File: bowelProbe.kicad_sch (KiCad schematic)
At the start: 52 parts, among them J10 Conn_01x01, J11 Conn_01x01, J12 Conn_01x01, J13 Conn_01x01, J2 Conn_01x01, J3 Conn_01x01, J4 Conn_01x01, J5 Conn_01x01, J6 Conn_01x01, J7 Conn_01x01, J8 Conn_01x01, J9 Conn_01x01, U1 MAX038CPP, U2 OPA2134PA, U3 MCP6002-E/P, U4 TL072ACP

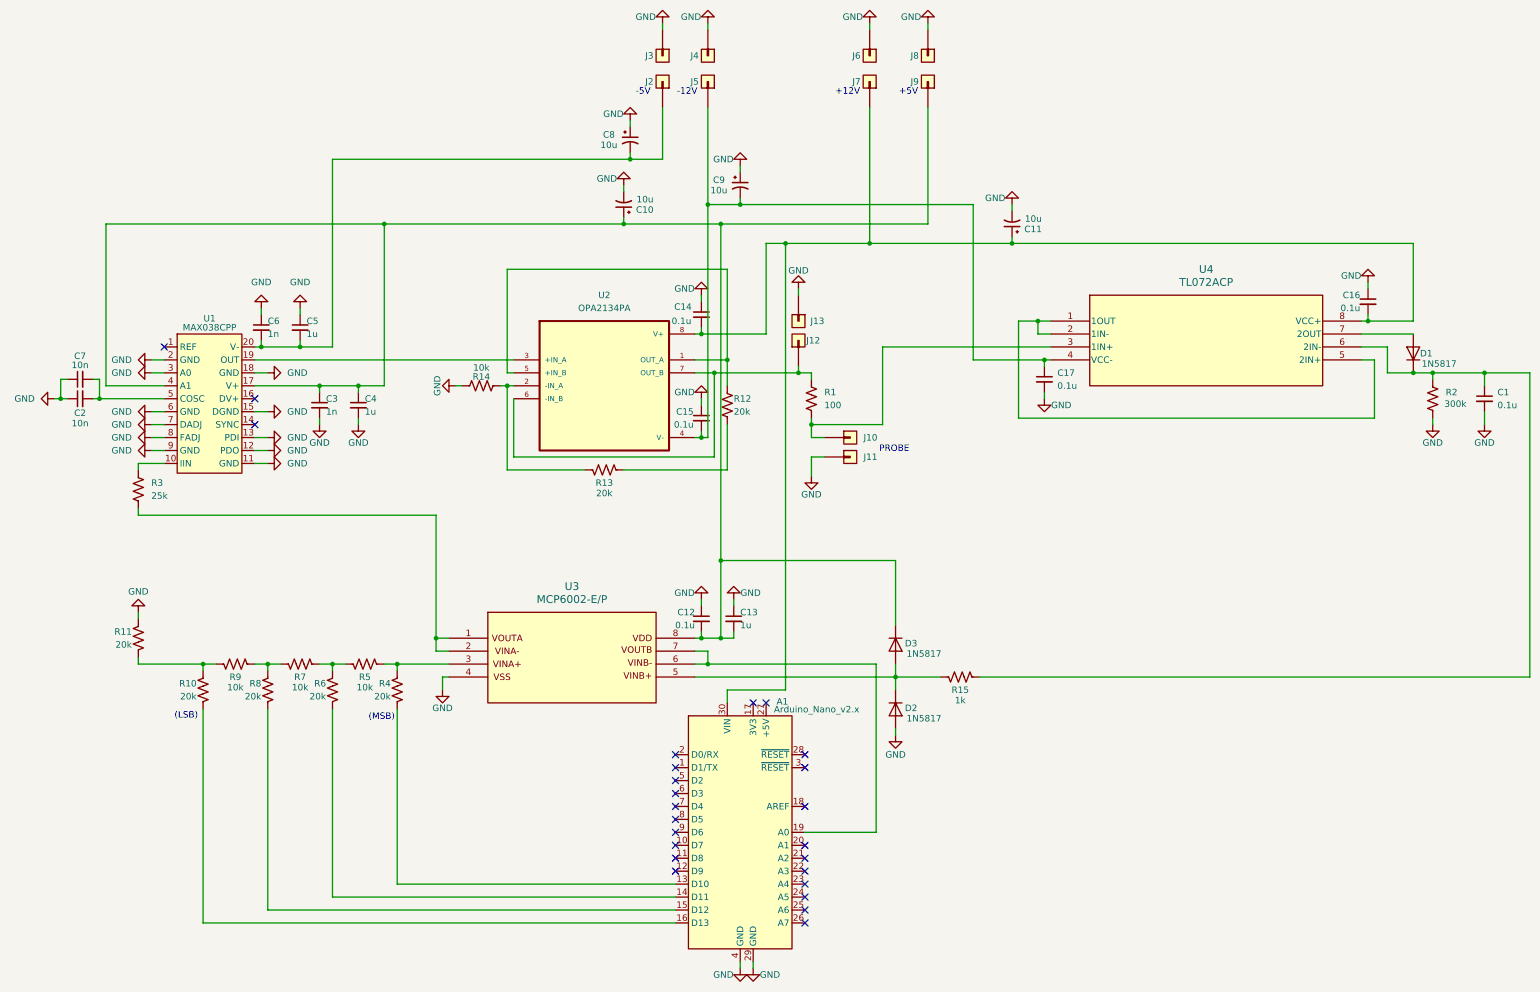
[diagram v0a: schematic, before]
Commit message: PCB Passed Final Check
Updated PCB reference designators (both in schematic and layout). Gave final check to ensure proper PCB layout and routing.
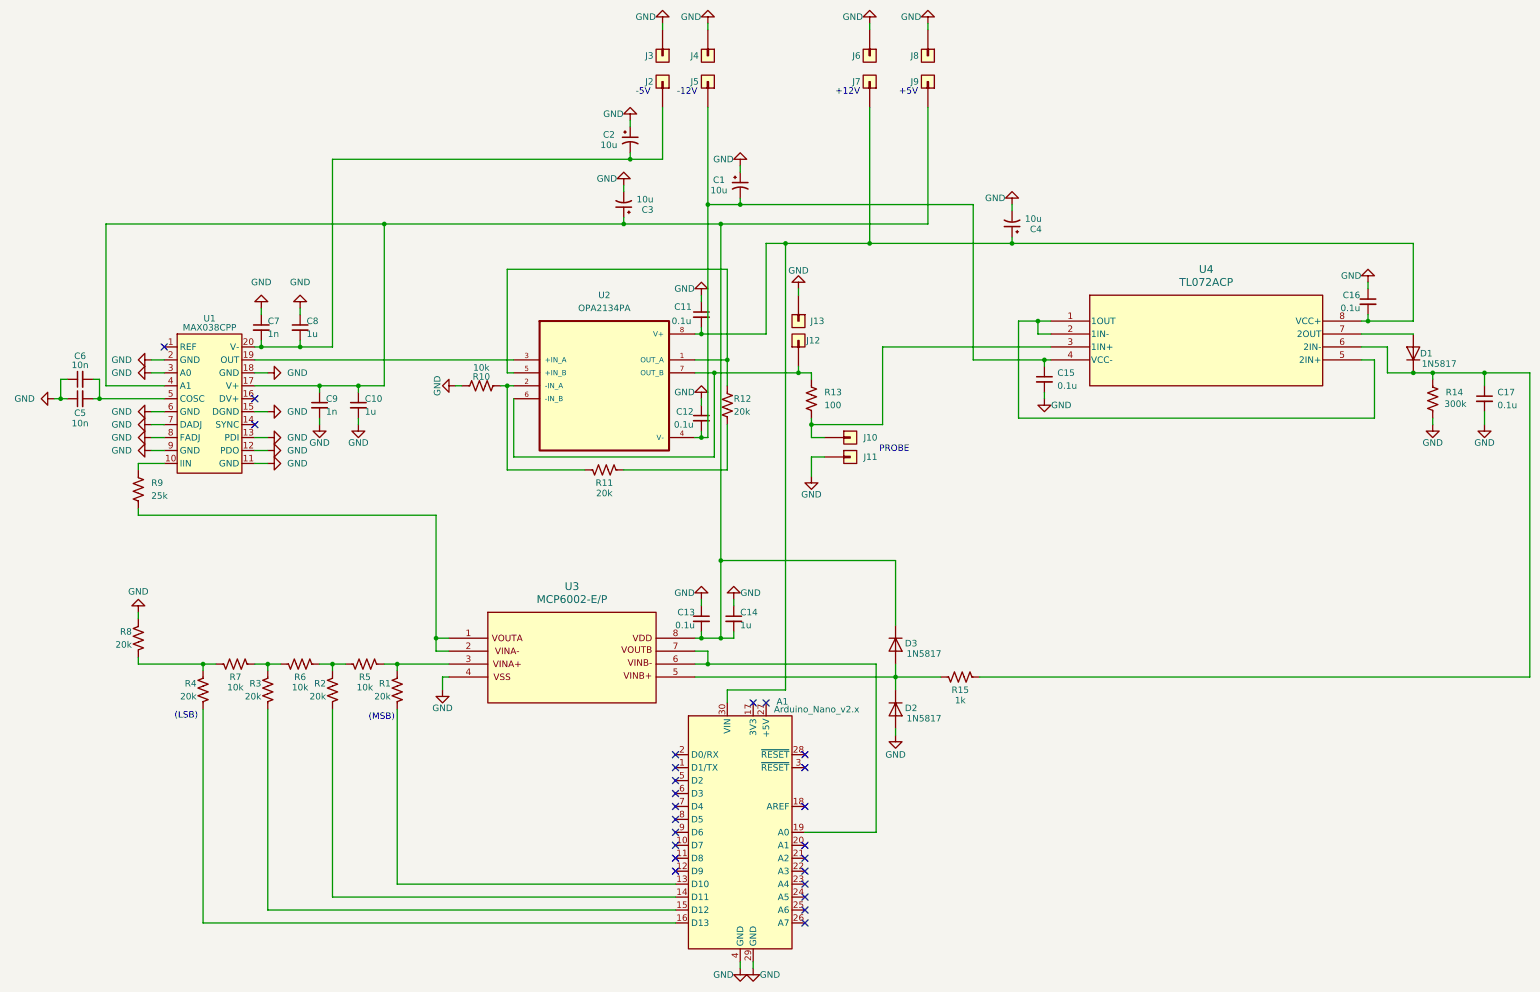
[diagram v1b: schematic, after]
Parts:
- renumbered C9 to C1, C4 to C10, C14 to C11, C15 to C12, C12 to C13, C13 to C14, C17 to C15, C1 to C17, C8 to C2, C10 to C3, C11 to C4, C2 to C5, C7 to C6, C6 to C7, C5 to C8, C3 to C9, R4 to R1, R14 to R10, R13 to R11, R1 to R13, R2 to R14, R6 to R2, R8 to R3, R10 to R4, R7 to R6, R9 to R7, R11 to R8, R3 to R9
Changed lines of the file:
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@@
 		(on_board yes)
 		(dnp no)
-		(property "Reference" "R4"
+		(property "Reference" "R1"
 			(at 130.81 147.32 0)
 			(effects
@@
 			(project "bowelProbe"
 				(path "/b054b76f-bc06-48fe-994a-b07fc1433235"
-					(reference "R4")
+					(reference "R1")
 					(unit 1)
 				)
@@
 		(on_board yes)
 		(dnp no)
-		(property "Reference" "C11"
+		(property "Reference" "C4"
 			(at 258.572 58.166 0)
 			(effects
@@
 			(project "bowelProbe"
 				(path "/b054b76f-bc06-48fe-994a-b07fc1433235"
-					(reference "C11")
+					(reference "C4")
 					(unit 1)
 				)
@@
 		(on_board yes)
 		(dnp no)
-		(property "Reference" "C6"
+		(property "Reference" "C7"
 			(at 106.68 76.2 0)
 			(effects
@@
 			(project "bowelProbe"
 				(path "/b054b76f-bc06-48fe-994a-b07fc1433235"
-					(reference "C6")
+					(reference "C7")
 					(unit 1)
 				)
@@
 		(on_board yes)
 		(dnp no)
-		(property "Reference" "C10"
+		(property "Reference" "C3"
 			(at 182.372 54.356 0)
 			(effects
@@
 			(project "bowelProbe"
 				(path "/b054b76f-bc06-48fe-994a-b07fc1433235"
-					(reference "C10")
+					(reference "C3")
 					(unit 1)
 				)
@@
 		(on_board yes)
 		(dnp no)
-		(property "Reference" "R11"
+		(property "Reference" "R8"
 			(at 80.01 137.16 0)
 			(effects
@@
 			(project "bowelProbe"
 				(path "/b054b76f-bc06-48fe-994a-b07fc1433235"
-					(reference "R11")
+					(reference "R8")
 					(unit 1)
 				)
@@
 		(on_board yes)
 		(dnp no)
-		(property "Reference" "R7"
+		(property "Reference" "R6"
 			(at 113.03 146.05 90)
 			(effects
@@
 			(project "bowelProbe"
 				(path "/b054b76f-bc06-48fe-994a-b07fc1433235"
-					(reference "R7")
+					(reference "R6")
 					(unit 1)
 				)
@@
 		(on_board yes)
 		(dnp no)
-		(property "Reference" "R13"
+		(property "Reference" "R11"
 			(at 172.72 107.95 90)
 			(effects
@@
 			(project "bowelProbe"
 				(path "/b054b76f-bc06-48fe-994a-b07fc1433235"
-					(reference "R13")
+					(reference "R11")
 					(unit 1)
 				)
@@
 		(on_board yes)
 		(dnp no)
-		(property "Reference" "C9"
+		(property "Reference" "C1"
 			(at 194.056 48.514 0)
 			(effects
@@
 			(project "bowelProbe"
 				(path "/b054b76f-bc06-48fe-994a-b07fc1433235"
-					(reference "C9")
+					(reference "C1")
 					(unit 1)
 				)
@@
 		(dnp no)
 		(fields_autoplaced yes)
-		(property "Reference" "C17"
+		(property "Reference" "C15"
 			(at 261.62 86.3662 0)
 			(effects
@@
 			(project "bowelProbe"
 				(path "/b054b76f-bc06-48fe-994a-b07fc1433235"
-					(reference "C17")
+					(reference "C15")
 					(unit 1)
 				)
@@
 		(dnp no)
 		(fields_autoplaced yes)
-		(property "Reference" "C1"
+		(property "Reference" "C17"
 			(at 347.98 90.1762 0)
 			(effects
@@
 			(project "bowelProbe"
 				(path "/b054b76f-bc06-48fe-994a-b07fc1433235"
-					(reference "C1")
+					(reference "C17")
 					(unit 1)
 				)
@@
 		(on_board yes)
 		(dnp no)
-		(property "Reference" "C4"
+		(property "Reference" "C10"
 			(at 125.73 91.44 0)
 			(effects
@@
 			(project "bowelProbe"
 				(path "/b054b76f-bc06-48fe-994a-b07fc1433235"
-					(reference "C4")
+					(reference "C10")
 					(unit 1)
 				)
@@
 		(dnp no)
 		(fields_autoplaced yes)
-		(property "Reference" "R3"
+		(property "Reference" "R9"
 			(at 83.82 107.9499 0)
 			(effects
@@
 			(project "bowelProbe"
 				(path "/b054b76f-bc06-48fe-994a-b07fc1433235"
-					(reference "R3")
+					(reference "R9")
 					(unit 1)
 				)
@@
 		(on_board yes)
 		(dnp no)
-		(property "Reference" "C15"
+		(property "Reference" "C12"
 			(at 190.246 93.98 0)
 			(effects
@@
 			(project "bowelProbe"
 				(path "/b054b76f-bc06-48fe-994a-b07fc1433235"
-					(reference "C15")
+					(reference "C12")
 					(unit 1)
 				)
@@
 		(on_board yes)
 		(dnp no)
-		(property "Reference" "R2"
+		(property "Reference" "R14"
 			(at 337.82 90.1699 0)
 			(effects
@@
 			(project "bowelProbe"
 				(path "/b054b76f-bc06-48fe-994a-b07fc1433235"
-					(reference "R2")
+					(reference "R14")
 					(unit 1)
 				)
@@
 		(on_board yes)
 		(dnp no)
-		(property "Reference" "R8"
+		(property "Reference" "R3"
 			(at 105.41 147.32 0)
 			(effects
@@
 			(project "bowelProbe"
 				(path "/b054b76f-bc06-48fe-994a-b07fc1433235"
-					(reference "R8")
+					(reference "R3")
 					(unit 1)
 				)
@@
 		(on_board yes)
 		(dnp no)
-		(property "Reference" "C13"
+		(property "Reference" "C14"
 			(at 199.39 133.35 0)
 			(effects
@@
 			(project "bowelProbe"
 				(path "/b054b76f-bc06-48fe-994a-b07fc1433235"
-					(reference "C13")
+					(reference "C14")
 					(unit 1)
 				)
@@
 		(on_board yes)
 		(dnp no)
-		(property "Reference" "C2"
+		(property "Reference" "C5"
 			(at 69.85 94.234 90)
 			(effects
@@
 			(project "bowelProbe"
 				(path "/b054b76f-bc06-48fe-994a-b07fc1433235"
-					(reference "C2")
+					(reference "C5")
 					(unit 1)
 				)
@@
 		(on_board yes)
 		(dnp no)
-		(property "Reference" "R6"
+		(property "Reference" "R2"
 			(at 118.11 147.32 0)
 			(effects
@@
 			(project "bowelProbe"
 				(path "/b054b76f-bc06-48fe-994a-b07fc1433235"
-					(reference "R6")
+					(reference "R2")
 					(unit 1)
 				)
@@
 		(on_board yes)
 		(dnp no)
-		(property "Reference" "C7"
+		(property "Reference" "C6"
 			(at 69.85 83.058 90)
 			(effects
@@
 			(project "bowelProbe"
 				(path "/b054b76f-bc06-48fe-994a-b07fc1433235"
-					(reference "C7")
+					(reference "C6")
 					(unit 1)
 				)
@@
 		(on_board yes)
 		(dnp no)
-		(property "Reference" "C14"
+		(property "Reference" "C11"
 			(at 186.436 73.406 0)
 			(effects
@@
 			(project "bowelProbe"
 				(path "/b054b76f-bc06-48fe-994a-b07fc1433235"
-					(reference "C14")
+					(reference "C11")
 					(unit 1)
 				)
@@
 		(on_board yes)
 		(dnp no)
-		(property "Reference" "C8"
+		(property "Reference" "C2"
 			(at 172.466 39.624 0)
 			(effects
@@
 			(project ""
 				(path "/b054b76f-bc06-48fe-994a-b07fc1433235"
-					(reference "C8")
+					(reference "C2")
 					(unit 1)
 				)
@@
 		(on_board yes)
 		(dnp no)
-		(property "Reference" "C12"
+		(property "Reference" "C13"
 			(at 190.5 133.35 0)
 			(effects
@@
 			(project "bowelProbe"
 				(path "/b054b76f-bc06-48fe-994a-b07fc1433235"
-					(reference "C12")
+					(reference "C13")
 					(unit 1)
 				)
@@
 		(dnp no)
 		(fields_autoplaced yes)
-		(property "Reference" "R1"
+		(property "Reference" "R13"
 			(at 215.9 90.1699 0)
 			(effects
@@
 			(project ""
 				(path "/b054b76f-bc06-48fe-994a-b07fc1433235"
-					(reference "R1")
+					(reference "R13")
 					(unit 1)
 				)
@@
 		(on_board yes)
 		(dnp no)
-		(property "Reference" "C5"
+		(property "Reference" "C8"
 			(at 114.3 76.2 0)
 			(effects
@@
 			(project "bowelProbe"
 				(path "/b054b76f-bc06-48fe-994a-b07fc1433235"
-					(reference "C5")
+					(reference "C8")
 					(unit 1)
 				)
@@
 		(on_board yes)
 		(dnp no)
-		(property "Reference" "R10"
+		(property "Reference" "R4"
 			(at 92.71 147.32 0)
 			(effects
@@
 			(project "bowelProbe"
 				(path "/b054b76f-bc06-48fe-994a-b07fc1433235"
-					(reference "R10")
+					(reference "R4")
 					(unit 1)
 				)
@@
 		(on_board yes)
 		(dnp no)
-		(property "Reference" "C3"
+		(property "Reference" "C9"
 			(at 118.11 91.44 0)
 			(effects
@@
 			(project "bowelProbe"
 				(path "/b054b76f-bc06-48fe-994a-b07fc1433235"
-					(reference "C3")
+					(reference "C9")
 					(unit 1)
 				)
@@
 		(on_board yes)
 		(dnp no)
-		(property "Reference" "R9"
+		(property "Reference" "R7"
 			(at 100.33 146.05 90)
 			(effects
@@
 			(project "bowelProbe"
 				(path "/b054b76f-bc06-48fe-994a-b07fc1433235"
-					(reference "R9")
+					(reference "R7")
 					(unit 1)
 				)
@@
 		(on_board yes)
 		(dnp no)
-		(property "Reference" "R14"
+		(property "Reference" "R10"
 			(at 148.59 87.122 90)
 			(effects
@@
 			(project "bowelProbe"
 				(path "/b054b76f-bc06-48fe-994a-b07fc1433235"
-					(reference "R14")
+					(reference "R10")
 					(unit 1)
 				)
